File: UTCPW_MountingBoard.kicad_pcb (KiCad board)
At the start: 2 copper layers, 49.4 x 44.5 mm, 10 parts, among them U1 UltrathinT2SLCPW

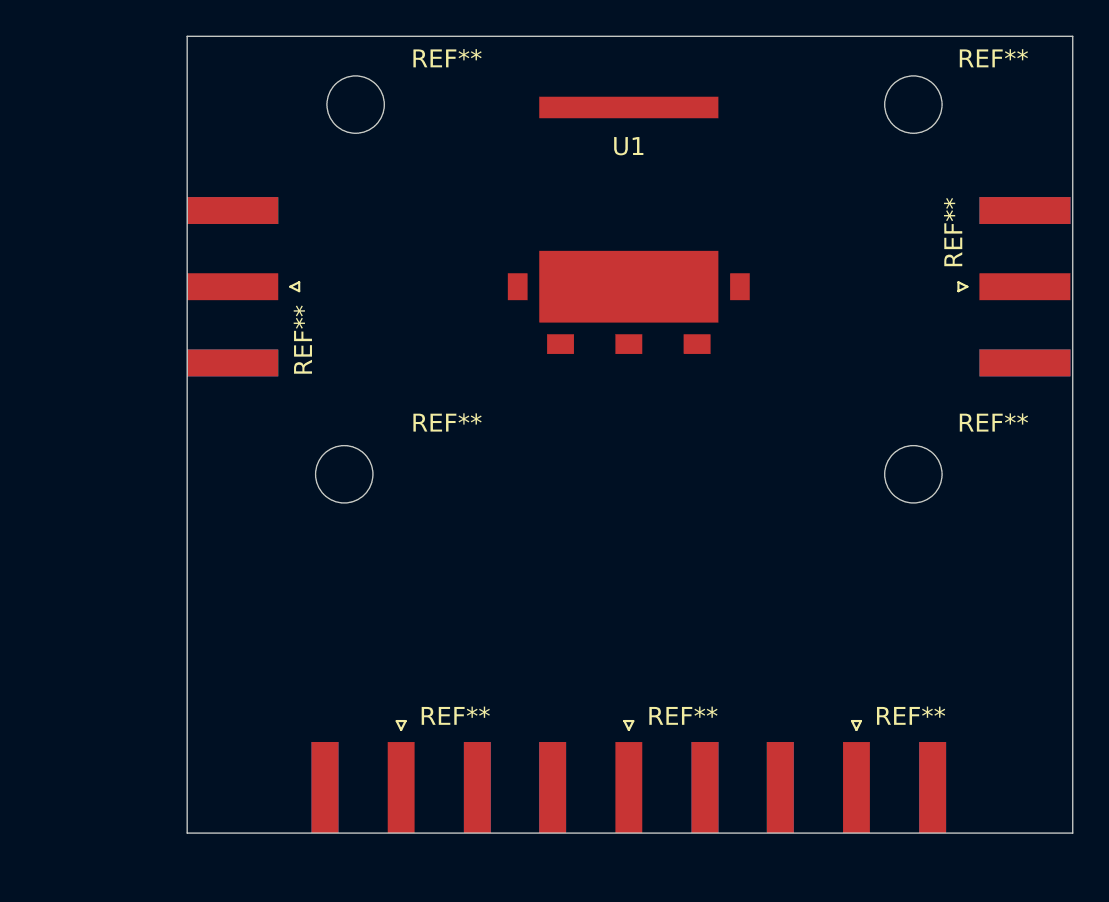
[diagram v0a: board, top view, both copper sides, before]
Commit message: Shrunken board
Shrunk board size, same Amphenol connector footprint although will not be using 132289 anymore.
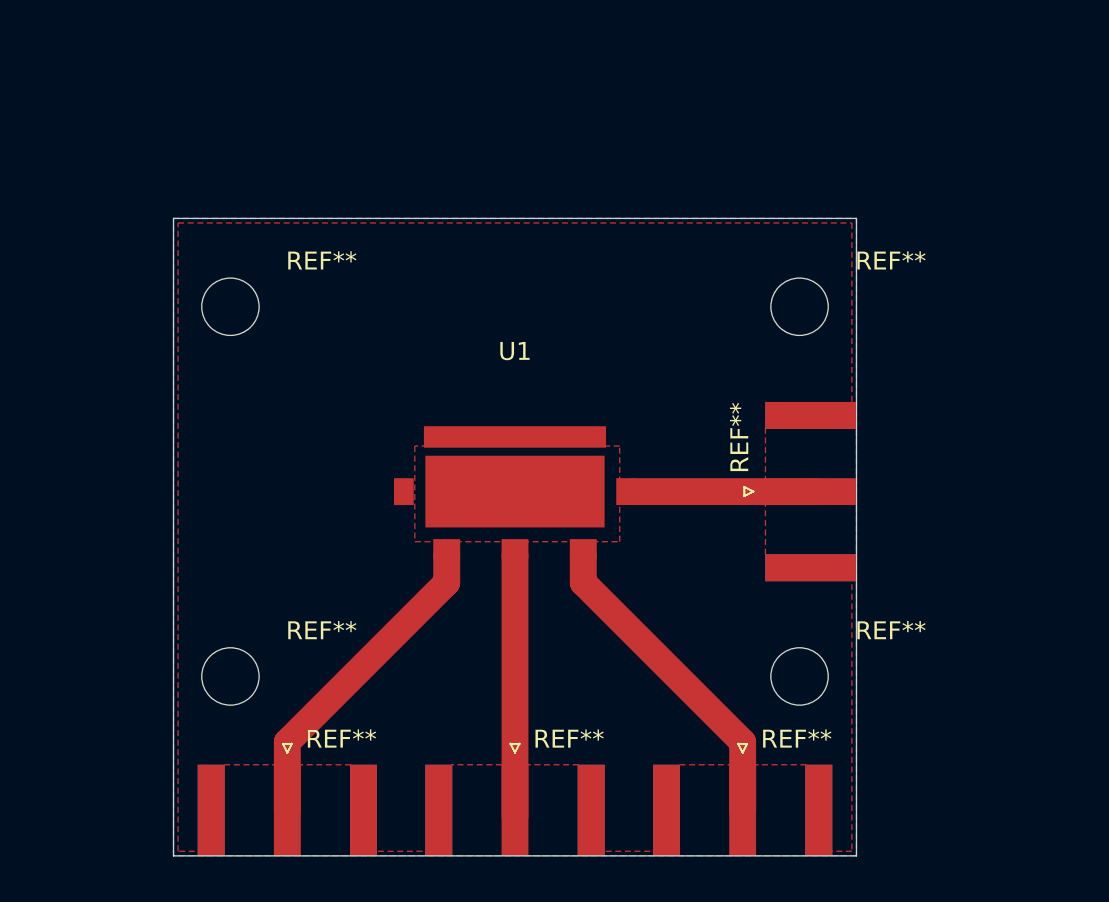
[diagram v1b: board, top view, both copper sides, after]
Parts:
- removed the REF** at (148.6, 80.0)
- removed the REF** at (146.1, 118.1)
- removed the REF** at (133.3, 118.1)
- removed the REF** at (120.7, 118.1)
- removed the REF** at (155.4, 90.2)
- removed the REF** at (111.3, 90.2)
- removed the REF** at (148.6, 100.3)
- removed the REF** at (118.1, 100.3)
- added REF**: SMA_Amphenol_132289_EdgeMount, Connector_Coaxial:SMA_Amphenol_132289_EdgeMount, F.Cu at (143.5, 101.6)
- added REF**: SMA_Amphenol_132289_EdgeMount, Connector_Coaxial:SMA_Amphenol_132289_EdgeMount, F.Cu at (139.7, 119.4)
- added REF**: SMA_Amphenol_132289_EdgeMount, Connector_Coaxial:SMA_Amphenol_132289_EdgeMount, F.Cu at (127.0, 119.4)
- added REF**: SMA_Amphenol_132289_EdgeMount, Connector_Coaxial:SMA_Amphenol_132289_EdgeMount, F.Cu at (114.3, 119.4)
- added REF**: MountingHole_2.7mm, MountingHole:MountingHole_2.7mm, F.Cu at (142.9, 91.3)
- added REF**: MountingHole_2.7mm, MountingHole:MountingHole_2.7mm, F.Cu at (142.9, 111.9)
- added REF**: MountingHole_2.7mm, MountingHole:MountingHole_2.7mm, F.Cu at (111.1, 111.9)
- moved REF** 13.3 mm to (111.1, 91.3)
- moved U1 13.1 mm to (127.0, 101.6)
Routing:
- net /Dev2: track 0.00 -> 17.9 mm
- net /Dev4: track 0.00 -> 17.9 mm
- net /Dev3: track 0.00 -> 14.6 mm
- net /Dev5: track 0.00 -> 10.3 mm
- added copper zone on B.Cu, net /GND
- added copper zone on F.Cu, net /GND
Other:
- board size 49.4 x 44.5 mm -> 38.1 x 35.6 mm

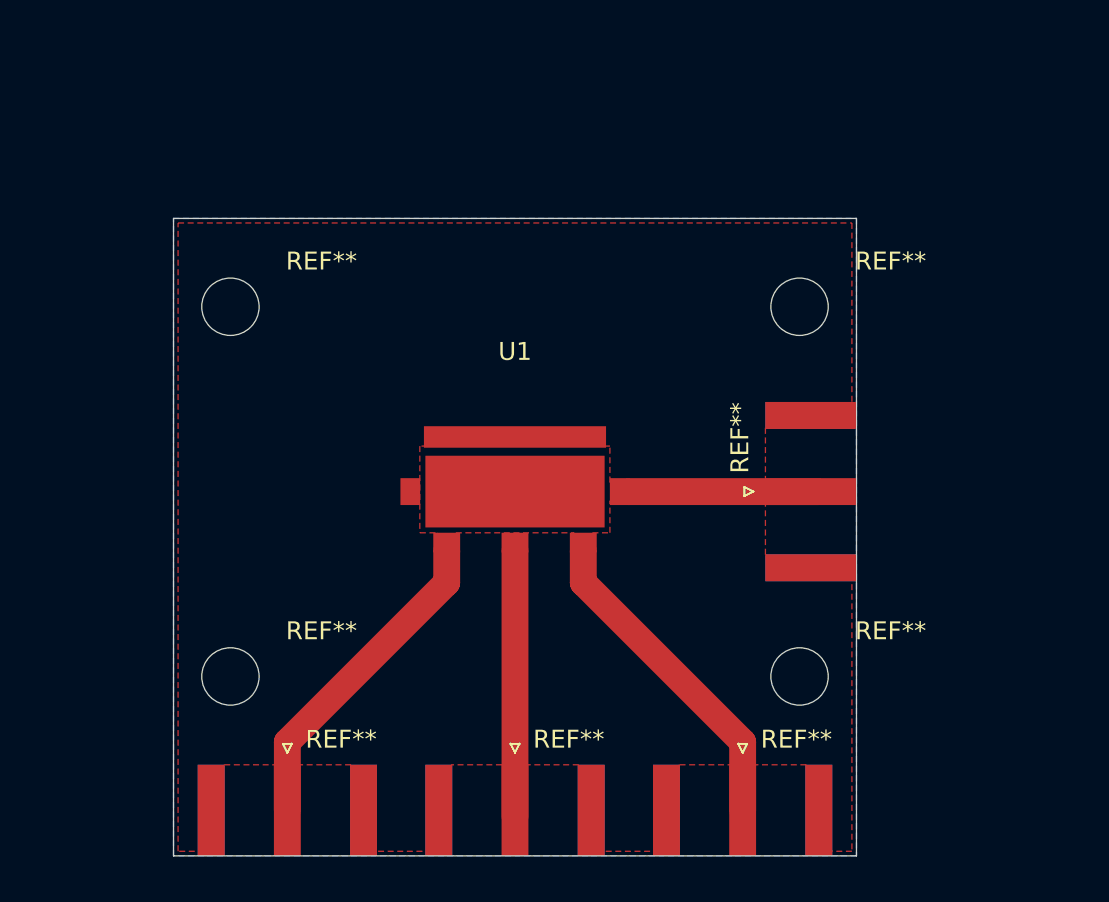
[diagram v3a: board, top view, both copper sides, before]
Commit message: 45deg cut metal
Reduce metal use in regions far from signal transfer (just a simple 45 degree cut). Good luck!
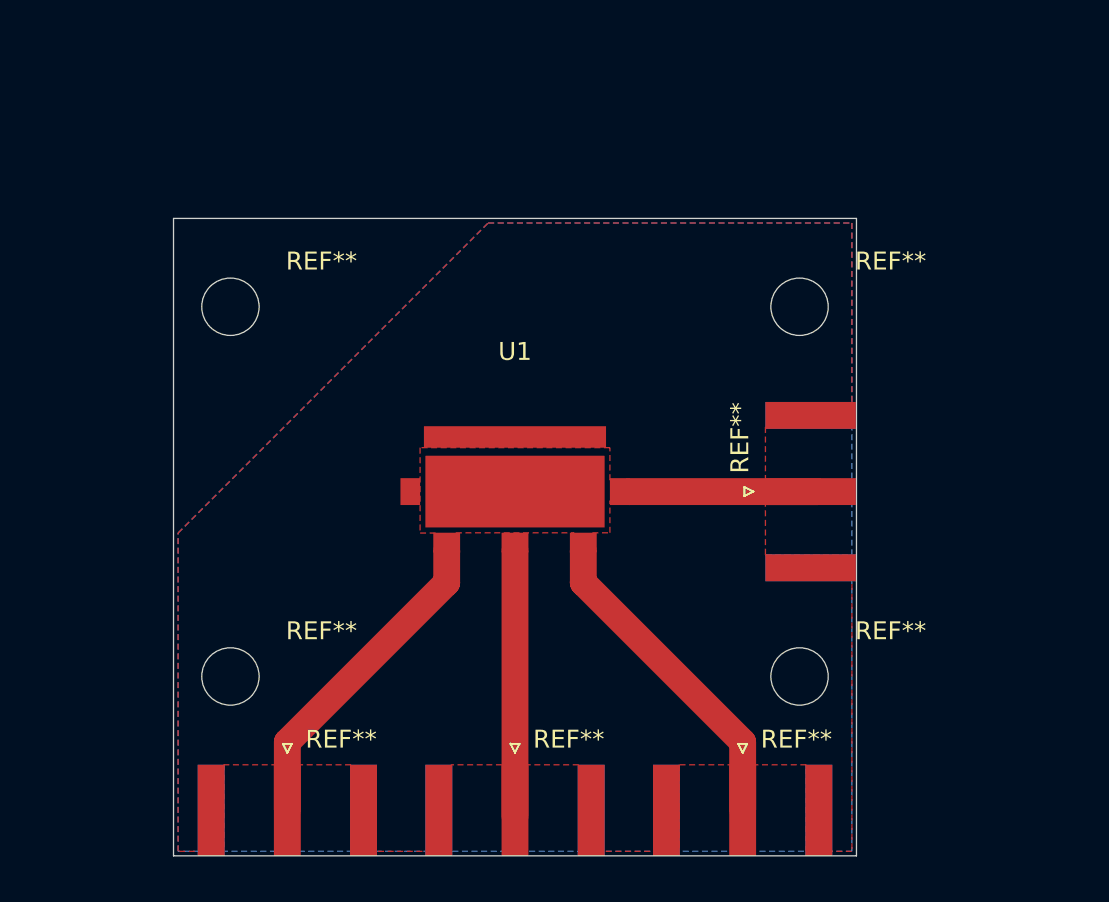
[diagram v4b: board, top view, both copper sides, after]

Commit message: Lib Relink and Footprint Updates
Relinked a few libraries
Updated footprints for the sample strip
Need to figure out filled zones... again
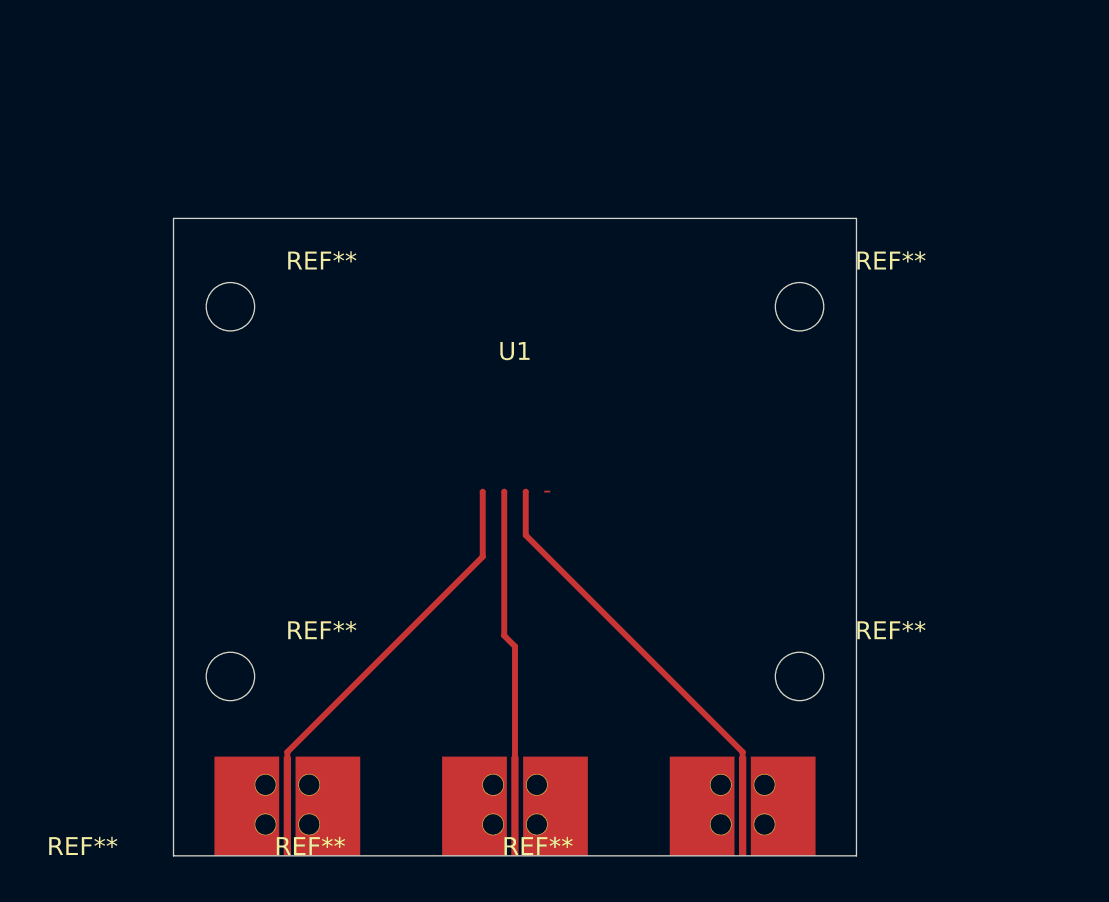
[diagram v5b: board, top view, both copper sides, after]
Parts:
- removed the REF** at (143.5, 101.6)
- removed the REF** at (139.7, 119.4)
- removed the REF** at (127.0, 119.4)
- removed the REF** at (114.3, 119.4)
- added REF**: 901-10510-2, UTMIR_Devices:901-10510-2, F.Cu at (139.7, 121.9)
- added REF**: 901-10510-2, UTMIR_Devices:901-10510-2, F.Cu at (127.0, 121.9)
- added REF**: 901-10510-2, UTMIR_Devices:901-10510-2, F.Cu at (114.3, 121.9)
- U1: value UltrathinT2SLCPW -> UTCPW_SampleStrip; footprint UTMIR_Devices:UltrathinT2SLCPW -> UTMIR_Devices:UTCPW_SampleStrip
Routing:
- net /Dev1: track 0.00 -> 22.1 mm
- net /Dev4: track 18.2 -> 0.00 mm
- net /Dev5: track 10.6 -> 0.00 mm
- net /Dev3: track 14.8 -> 22.6 mm
- removed copper zone on B.Cu, net /GND
- removed copper zone on F.Cu, net /GND

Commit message: Updated Gerber
Initial version for the new board
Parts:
- moved REF** 0.60 mm to (126.4, 121.9)
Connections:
- REF** pad 2: (no net) -> /GND (x2)
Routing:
- net /Dev3: track 22.6 -> 25.2 mm
- net /Dev1: track 22.1 -> 24.0 mm
- added copper zone on B.Cu, net (none)
- added copper zone on F.Cu, net /GND
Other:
- net class Default removed
